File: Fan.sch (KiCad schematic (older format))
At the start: 9 parts

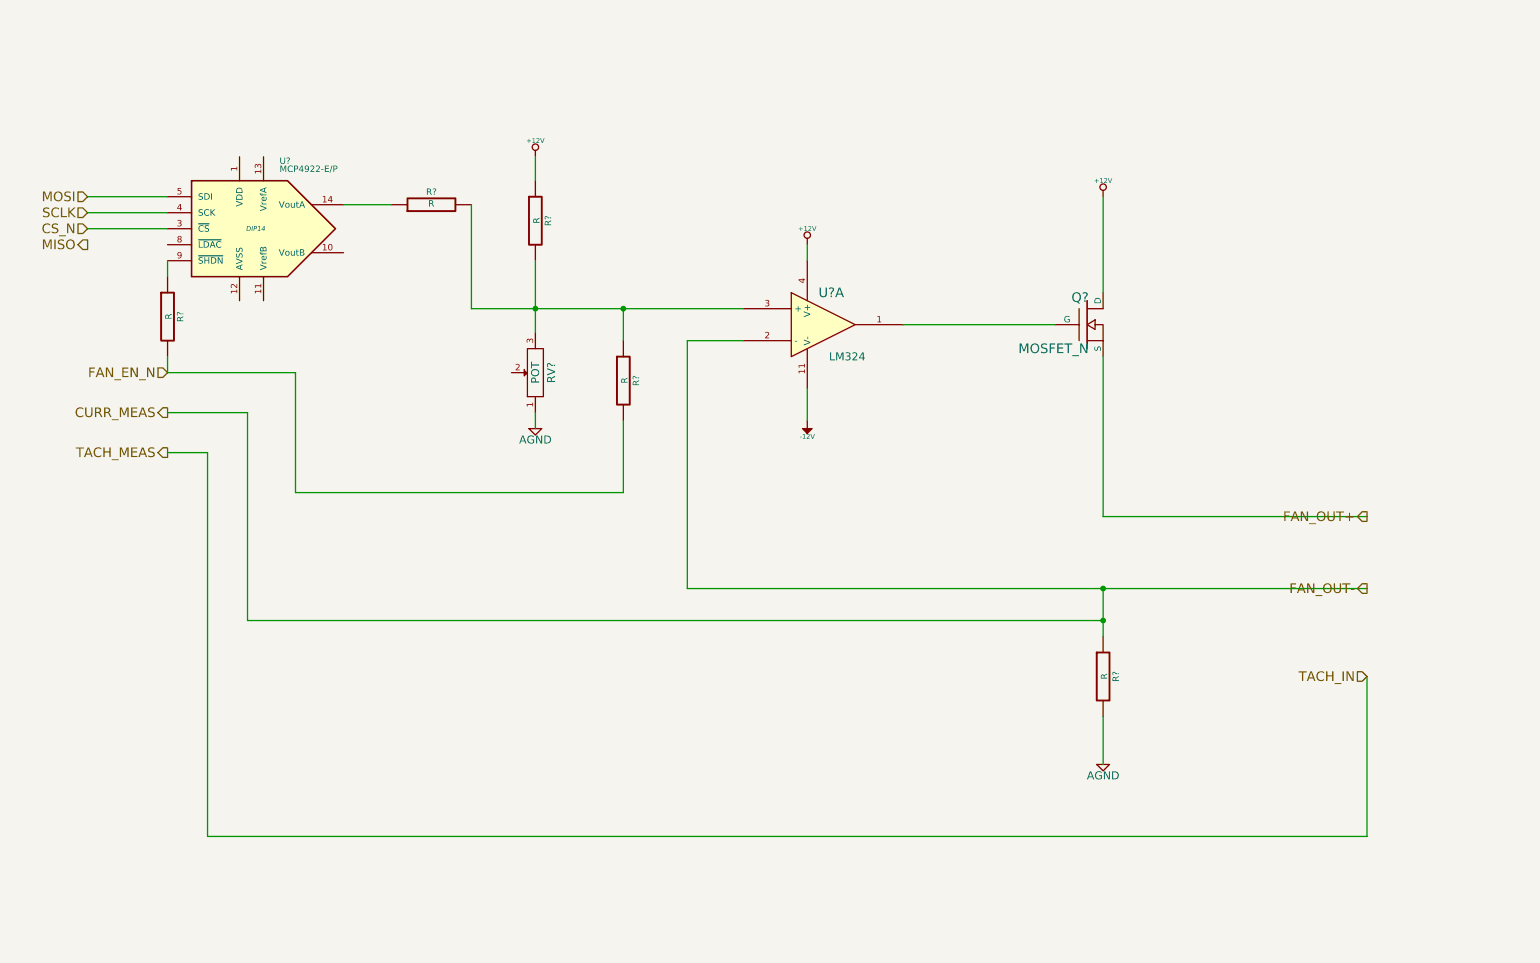
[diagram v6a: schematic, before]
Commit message: M3 U9
Revisiting the Current/Fan Module
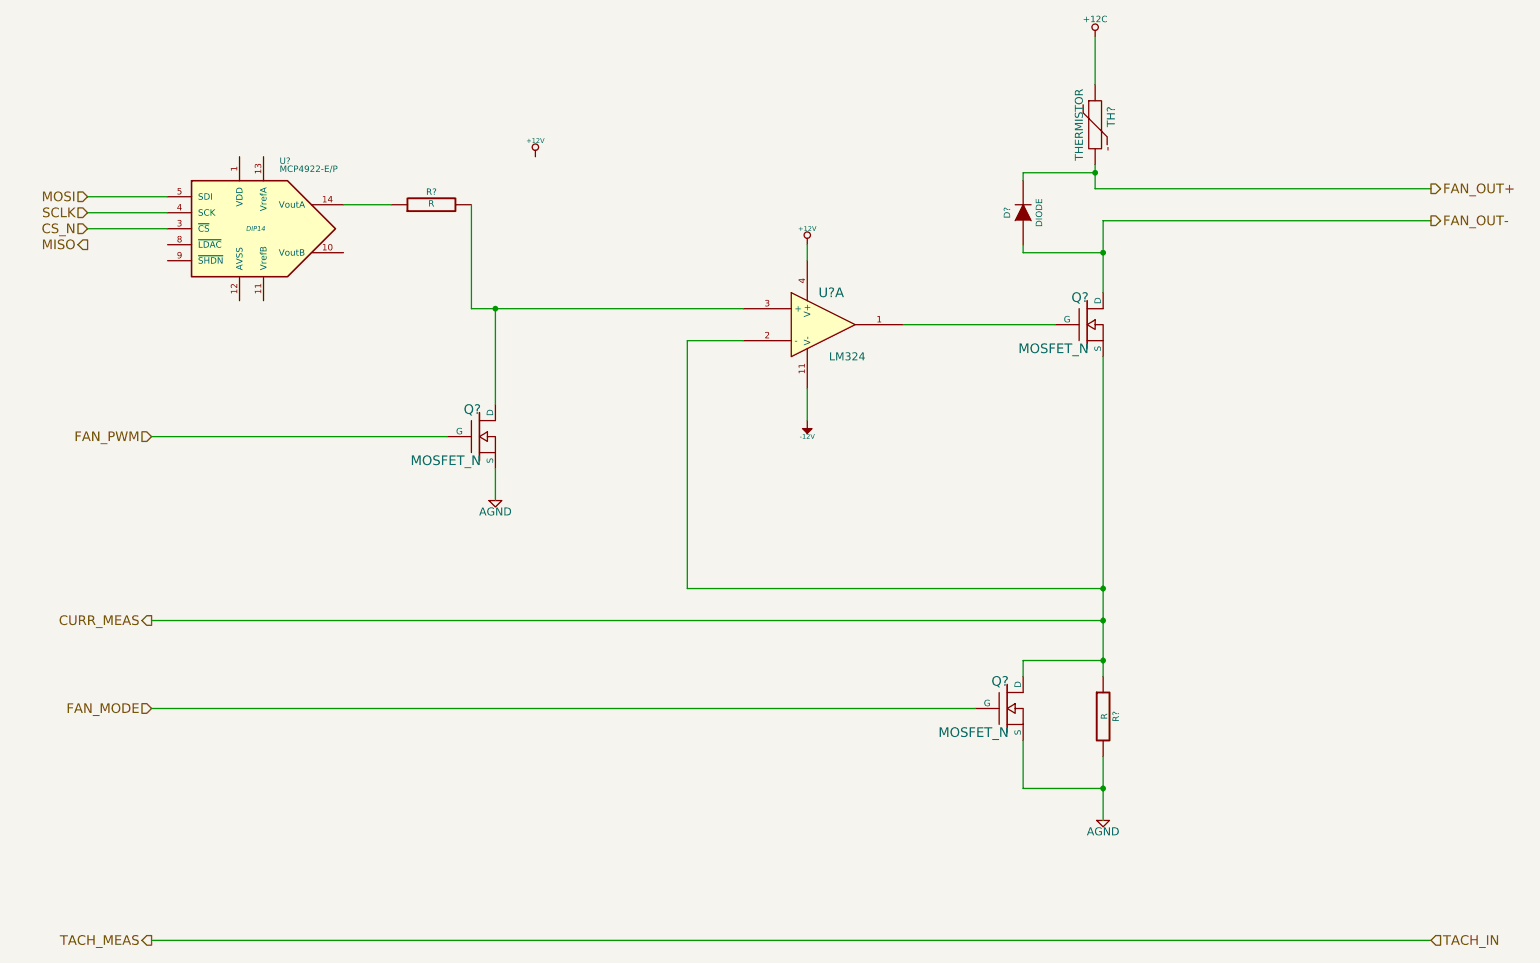
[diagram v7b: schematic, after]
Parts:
- removed R? (x3): R, ~, symbol R
- removed RV?: POT, ~, symbol POT
- added D?: DIODE, ~, symbol DIODE
- added Q? (x2): MOSFET_N, ~, symbol MOSFET_N
- added TH?: THERMISTOR, ~, symbol THERMISTOR
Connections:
- net +12V: no longer Q?.D
- net AGND: now also Q?.S, Q?.S
- net CURR_MEAS: now also Q?.S, Q?.D
- net FAN_OUT+: now also D?.2 (K), TH?.2; no longer Q?.S
- net at R?.2, U?.3 (+): now also Q?.D
- new net +12C: TH?.1
- new net FAN_MODE: Q?.G
- new net FAN_OUT-: D?.1 (A), Q?.D
- new net FAN_PWM: Q?.G
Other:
- moved on the sheet: R?
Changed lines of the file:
@@
 Comment4 ""
 $EndDescr
-Text HLabel 8950 3700 0    60   Output ~ 0
+Text HLabel 9350 1650 2    60   Output ~ 0
 FAN_OUT+
-Text HLabel 8950 4150 0    60   Output ~ 0
+Text HLabel 9350 1850 2    60   Output ~ 0
 FAN_OUT-
-Text HLabel 8950 4700 0    60   Input ~ 0
-TACH_IN
-Text HLabel 1450 3300 0    60   Output ~ 0
+Text HLabel 1350 6350 0    60   Output ~ 0
 TACH_MEAS
-Text HLabel 1450 2800 0    60   Input ~ 0
-FAN_EN_N
+Text HLabel 1350 3200 0    60   Input ~ 0
+FAN_PWM
 $Comp
 L LM324 U?
@@
 $EndComp
 $Comp
-L +12V #PWR?
-U 1 1 52F835C2
-P 7300 1700
-F 0 "#PWR?" H 7300 1650 20  0001 C CNN
-F 1 "+12V" H 7300 1800 30  0000 C CNN
-F 2 "" H 7300 1700 60  0000 C CNN
-F 3 "" H 7300 1700 60  0000 C CNN
-	1    7300 1700
-	1    0    0    -1
-$EndComp
-$Comp
 L R R?
 U 1 1 52F835E9
-P 7300 4700
-F 0 "R?" V 7380 4700 40  0000 C CNN
-F 1 "R" V 7307 4701 40  0000 C CNN
-F 2 "~" V 7230 4700 30  0000 C CNN
-F 3 "~" H 7300 4700 30  0000 C CNN
-	1    7300 4700
+P 7300 4950
+F 0 "R?" V 7380 4950 40  0000 C CNN
+F 1 "R" V 7307 4951 40  0000 C CNN
+F 2 "~" V 7230 4950 30  0000 C CNN
+F 3 "~" H 7300 4950 30  0000 C CNN
+	1    7300 4950
 	1    0    0    -1
 $EndComp
@@
 L AGND #PWR?
 U 1 1 52F83685
-P 7300 5250
-F 0 "#PWR?" H 7300 5250 40  0001 C CNN
-F 1 "AGND" H 7300 5180 50  0000 C CNN
-F 2 "" H 7300 5250 60  0000 C CNN
-F 3 "" H 7300 5250 60  0000 C CNN
-	1    7300 5250
+P 7300 5600
+F 0 "#PWR?" H 7300 5600 40  0001 C CNN
+F 1 "AGND" H 7300 5530 50  0000 C CNN
+F 2 "" H 7300 5600 60  0000 C CNN
+F 3 "" H 7300 5600 60  0000 C CNN
+	1    7300 5600
 	1    0    0    -1
 $EndComp
@@
 	6050 2500 7000 2500
 Wire Wire Line
-	7300 1700 7300 2300
-Wire Wire Line
-	7300 2700 7300 3700
-Wire Wire Line
-	7300 3700 8950 3700
-Wire Wire Line
-	4700 4150 8950 4150
-Wire Wire Line
-	7300 4150 7300 4450
-Wire Wire Line
-	7300 4950 7300 5250
-Wire Wire Line
 	4700 4150 4700 2600
 Wire Wire Line
@@
 Wire Wire Line
 	5450 2900 5450 3100
-$Comp
-L R R?
-U 1 1 52F836DA
-P 3750 1850
-F 0 "R?" V 3830 1850 40  0000 C CNN
-F 1 "R" V 3757 1851 40  0000 C CNN
-F 2 "~" V 3680 1850 30  0000 C CNN
-F 3 "~" H 3750 1850 30  0000 C CNN
-	1    3750 1850
-	1    0    0    -1
-$EndComp
 Wire Wire Line
 	3350 2400 5050 2400
-Wire Wire Line
-	3750 2100 3750 2550
-$Comp
-L POT RV?
-U 1 1 52F836FF
-P 3750 2800
-F 0 "RV?" H 3750 2700 50  0000 C CNN
-F 1 "POT" H 3750 2800 50  0000 C CNN
-F 2 "~" H 3750 2800 60  0000 C CNN
-F 3 "~" H 3750 2800 60  0000 C CNN
-	1    3750 2800
-	0    -1   -1   0
-$EndComp
-Connection ~ 3750 2400
 $Comp
 L AGND #PWR?
 U 1 1 52F83721
-P 3750 3150
-F 0 "#PWR?" H 3750 3150 40  0001 C CNN
-F 1 "AGND" H 3750 3080 50  0000 C CNN
-F 2 "" H 3750 3150 60  0000 C CNN
-F 3 "" H 3750 3150 60  0000 C CNN
-	1    3750 3150
-	1    0    0    -1
-$EndComp
-Wire Wire Line
-	3750 3050 3750 3150
+P 3500 3600
+F 0 "#PWR?" H 3500 3600 40  0001 C CNN
+F 1 "AGND" H 3500 3530 50  0000 C CNN
+F 2 "" H 3500 3600 60  0000 C CNN
+F 3 "" H 3500 3600 60  0000 C CNN
+	1    3500 3600
+	1    0    0    -1
+$EndComp
 $Comp
 L MCP4922-E/P U?
@@
 	1    0    0    -1
 $EndComp
-Wire Wire Line
-	8950 5700 8950 4700
-Wire Wire Line
-	8950 5700 1700 5700
-Wire Wire Line
-	1700 5700 1700 3300
-Text HLabel 1450 3050 0    60   Output ~ 0
+Text HLabel 1350 4350 0    60   Output ~ 0
 CURR_MEAS
 Wire Wire Line
-	7300 4350 1950 4350
+	1350 4350 7300 4350
 Connection ~ 7300 4350
-$Comp
-L R R?
-U 1 1 52F838A3
-P 4300 2850
-F 0 "R?" V 4380 2850 40  0000 C CNN
-F 1 "R" V 4307 2851 40  0000 C CNN
-F 2 "~" V 4230 2850 30  0000 C CNN
-F 3 "~" H 4300 2850 30  0000 C CNN
-	1    4300 2850
-	1    0    0    -1
-$EndComp
-Wire Wire Line
-	4300 2400 4300 2600
-Connection ~ 4300 2400
-Wire Wire Line
-	4300 3100 4300 3550
-Wire Wire Line
-	4300 3550 2250 3550
-Wire Wire Line
-	2250 3550 2250 2800
 $Comp
 L +12V #PWR?
@@
 	1    0    0    -1
 $EndComp
-Wire Wire Line
-	3750 1450 3750 1600
 $Comp
 L R R?
@@
 	950  1900 1450 1900
 $Comp
-L R R?
-U 1 1 52F83ABD
-P 1450 2450
-F 0 "R?" V 1530 2450 40  0000 C CNN
-F 1 "R" V 1457 2451 40  0000 C CNN
-F 2 "~" V 1380 2450 30  0000 C CNN
-F 3 "~" H 1450 2450 30  0000 C CNN
-	1    1450 2450
-	1    0    0    -1
-$EndComp
-Wire Wire Line
-	1700 3300 1450 3300
-Wire Wire Line
-	1950 4350 1950 3050
-Wire Wire Line
-	1950 3050 1450 3050
-Wire Wire Line
-	2250 2800 1450 2800
-Wire Wire Line
-	1450 2800 1450 2700
-Wire Wire Line
-	1450 2100 1450 2200
+L MOSFET_N Q?
+U 1 1 5300E019
+P 6700 4900
+F 0 "Q?" H 6710 5070 60  0000 R CNN
+F 1 "MOSFET_N" H 6710 4750 60  0000 R CNN
+F 2 "~" H 6700 4900 60  0000 C CNN
+F 3 "~" H 6700 4900 60  0000 C CNN
+	1    6700 4900
+	1    0    0    -1
+$EndComp
+$Comp
+L THERMISTOR TH?
+U 1 1 5300E263
+P 7250 1250
+F 0 "TH?" V 7350 1300 50  0000 C CNN
+F 1 "THERMISTOR" V 7150 1250 50  0000 C CNN
+F 2 "~" H 7250 1250 60  0000 C CNN
+F 3 "~" H 7250 1250 60  0000 C CNN
+	1    7250 1250
+	1    0    0    -1
+$EndComp
+Wire Wire Line
+	7250 700  7250 1000
+Wire Wire Line
+	7250 1500 7250 1650
+Wire Wire Line
+	7250 1650 9350 1650
+Wire Wire Line
+	7300 2300 7300 1850
+Wire Wire Line
+	7300 1850 9350 1850
+Wire Wire Line
+	7300 2050 6800 2050
+Connection ~ 7300 2050
+$Comp
+L DIODE D?
+U 1 1 5300E348
+P 6800 1800
+F 0 "D?" H 6800 1900 40  0000 C CNN
+F 1 "DIODE" H 6800 1700 40  0000 C CNN
+F 2 "~" H 6800 1800 60  0000 C CNN
+F 3 "~" H 6800 1800 60  0000 C CNN
+	1    6800 1800
+	0    -1   -1   0
+$EndComp
+Wire Wire Line
+	6800 2050 6800 2000
+Wire Wire Line
+	6800 1600 6800 1550
+Wire Wire Line
+	6800 1550 7250 1550
+Connection ~ 7250 1550
+Wire Wire Line
+	7300 4150 4700 4150
+Wire Wire Line
+	7300 2700 7300 4700
+Wire Wire Line
+	7300 5200 7300 5600
+Wire Wire Line
+	7300 5400 6800 5400
+Wire Wire Line
+	6800 5400 6800 5100
+Connection ~ 7300 5400
+Wire Wire Line
+	6800 4700 6800 4600
+Wire Wire Line
+	6800 4600 7300 4600
+Connection ~ 7300 4600
+$Comp
+L MOSFET_N Q?
+U 1 1 5300EAAC
+P 3400 3200
+F 0 "Q?" H 3410 3370 60  0000 R CNN
+F 1 "MOSFET_N" H 3410 3050 60  0000 R CNN
+F 2 "~" H 3400 3200 60  0000 C CNN
+F 3 "~" H 3400 3200 60  0000 C CNN
+	1    3400 3200
+	1    0    0    -1
+$EndComp
+Wire Wire Line
+	3500 3400 3500 3600
+Wire Wire Line
+	3500 3000 3500 2400
+Connection ~ 3500 2400
+Wire Wire Line
+	6500 4900 1350 4900
+Text HLabel 1350 4900 0    60   Input ~ 0
+FAN_MODE
+Wire Wire Line
+	1350 3200 3200 3200
+Text HLabel 9350 6350 2    60   Input ~ 0
+TACH_IN
+Wire Wire Line
+	1350 6350 9350 6350
+$Comp
+L +12C #PWR?
+U 1 1 53010826
+P 7250 700
+F 0 "#PWR?" H 7250 670 30  0001 C CNN
+F 1 "+12C" H 7250 810 40  0000 C CNN
+F 2 "" H 7250 700 60  0000 C CNN
+F 3 "" H 7250 700 60  0000 C CNN
+	1    7250 700
+	1    0    0    -1
+$EndComp
 $EndSCHEMATC
